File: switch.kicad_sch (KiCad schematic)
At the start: 5 parts, among them M1 LED, Q1 Q_Photo_NPN

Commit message: Add gerbers and assembly files
M  .gitignore
M  MyFootprints.pretty/MountingHole_2.2mm_M2_ISO7380_Pad.kicad_mod
M  MySymbols.kicad_sym
M  README.md
M  drawborder.py
A  jlcpcb/gerber/optical-keyboard-mx-B_Cu.gbl
A  jlcpcb/gerber/optical-keyboard-mx-B_Mask.gbs
A  jlcpcb/gerber/optical-keyboard-mx-B_Paste.gbp
A  jlcpcb/gerber/optical-keyboard-mx-B_Silkscreen.gbo
A  jlcpcb/gerber/optical-keyboard-mx-Edge_Cuts.gm1
A  jlcpcb/gerber/optical-keyboard-mx-F_Cu.gtl
A  jlcpcb/gerber/optical-keyboard-mx-F_Mask.gts
A  jlcpcb/gerber/optical-keyboard-mx-F_Paste.gtp
A  jlcpcb/gerber/optical-keyboard-mx-F_Silkscreen.gto
A  jlcpcb/gerber/optical-keyboard-mx-NPTH-drl_map.gbr
A  jlcpcb/gerber/optical-keyboard-mx-NPTH.drl
A  jlcpcb/gerber/optical-keyboard-mx-PTH-drl_map.gbr
A  jlcpcb/gerber/optical-keyboard-mx-PTH.drl
M  led_driver.kicad_sch
M  mounting-hw.kicad_sch
M  optical-keyboard-mx.kicad_pcb
M  optical-keyboard-mx.kicad_sch
M  placefp.py
M  switch-plate/.gitignore
A  switch-plate/jlcpcb/gerber/switch-plate-B_Cu.gbl
A  switch-plate/jlcpcb/gerber/switch-plate-B_Mask.gbs
A  switch-plate/jlcpcb/gerber/switch-plate-B_Paste.gbp
A  switch-plate/jlcpcb/gerber/switch-plate-B_Silkscreen.gbo
A  switch-plate/jlcpcb/gerber/switch-plate-Edge_Cuts.gm1
A  switch-plate/jlcpcb/gerber/switch-plate-F_Cu.gtl
A  switch-plate/jlcpcb/gerber/switch-plate-F_Mask.gts
A  switch-plate/jlcpcb/gerber/switch-plate-F_Paste.gtp
A  switch-plate/jlcpcb/gerber/switch-plate-F_Silkscreen.gto
A  switch-plate/jlcpcb/gerber/switch-plate-NPTH-drl_map.gbr
A  switch-plate/jlcpcb/gerber/switch-plate-NPTH.drl
A  switch-plate/jlcpcb/gerber/switch-plate-PTH-drl_map.gbr
A  switch-plate/jlcpcb/gerber/switch-plate-PTH.drl
M  switch-plate/switch-plate.kicad_pcb
M  switch-plate/switch-plate.kicad_prl
M  switch.kicad_sch
M  wrist-support/.gitignore
A  wrist-support/jlcpcb/gerber/wrist-support-B_Cu.gbl
A  wrist-support/jlcpcb/gerber/wrist-support-B_Mask.gbs
A  wrist-support/jlcpcb/gerber/wrist-support-B_Paste.gbp
A  wrist-support/jlcpc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
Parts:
- RL1: LCSC C4190 -> C22843
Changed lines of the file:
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@@
       (effects (font (size 0.5 0.5)) hide)
     )
-    (property "LCSC" "C4190" (id 5) (at 93.98 54.61 0)
+    (property "LCSC" "C22843" (id 5) (at 93.98 54.61 0)
       (effects (font (size 0.5 0.5)) hide)
     )

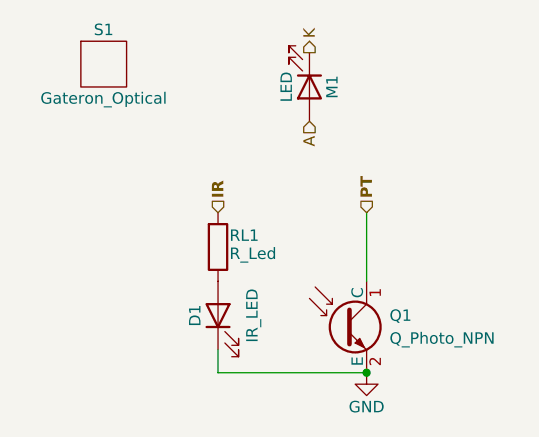
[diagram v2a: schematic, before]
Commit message: updated part numbers for jlcpcb
M  MySymbols.kicad_sym
M  drawborder.py
M  optical-keyboard-mx.kicad_sch
M  switch.kicad_sch
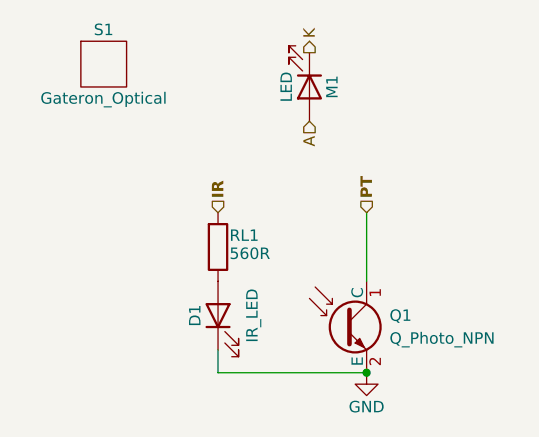
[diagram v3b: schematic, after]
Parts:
- RL1: value R_Led -> 560R; LCSC C22843 -> C23204
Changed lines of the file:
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@@
       (effects (font (size 1.27 1.27)) (justify left))
     )
-    (property "Value" "R_Led" (id 1) (at 91.44 58.42 0)
+    (property "Value" "560R" (id 1) (at 91.44 58.42 0)
       (effects (font (size 1.27 1.27)) (justify left top))
     )
@@
       (effects (font (size 0.5 0.5)) hide)
     )
-    (property "LCSC" "C22843" (id 5) (at 93.98 54.61 0)
+    (property "LCSC" "C23204" (id 5) (at 93.98 54.61 0)
       (effects (font (size 0.5 0.5)) hide)
     )
